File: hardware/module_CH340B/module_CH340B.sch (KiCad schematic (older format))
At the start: 5 parts, among them J1 USB-ID

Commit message: added usb input connections
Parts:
- J1: footprint (none) -> SquantorUsb:USB-muB-SMD_TH
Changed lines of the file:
@@
 F 0 "J1" H 1200 1250 50  0000 C CNN
 F 1 "USB-ID" H 1200 650 50  0000 C CNN
-F 2 "" H 1350 1000 60  0001 C CNN
+F 2 "SquantorUsb:USB-muB-SMD_TH" H 1350 1000 60  0001 C CNN
 F 3 "" H 1350 1000 60  0001 C CNN
 	1    1200 950

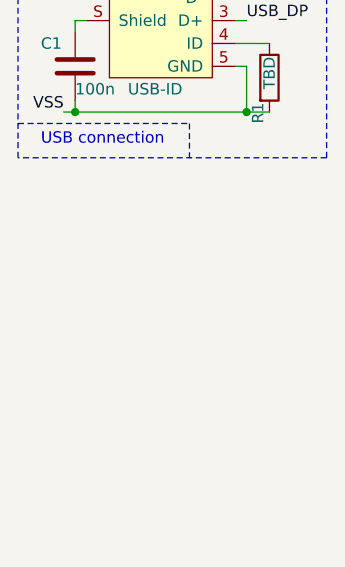
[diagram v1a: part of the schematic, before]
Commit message: added VBUS filtering
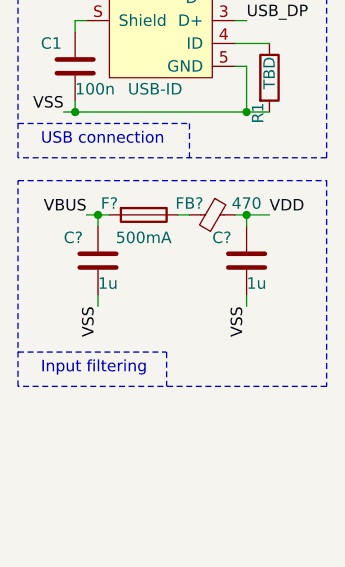
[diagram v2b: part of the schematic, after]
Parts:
- added C?: 1u, SquantorRcl:C_0603, symbol Device:C
- added C?: 1u, SquantorRcl:C_0805, symbol Device:C
- added F?: 500mA, SquantorRcl:R_0603_hand, symbol Device:Fuse
- added FB?: 470, SquantorRcl:L_0603, symbol Device:Ferrite_Bead_Small
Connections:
- net VBUS: now also C?.1, F?.2
- net VSS: now also C?.2, C?.2
- new net: F?.1, FB?.2
- new net VDD: C?.1, FB?.1
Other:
- note added: "Input filtering"
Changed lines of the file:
@@
 Wire Notes Line
 	1350 1400 1350 1550
+$Comp
+L Device:C C?
+U 1 1 5EE197E8
+P 950 2000
+F 0 "C?" H 800 2100 50  0000 L CNN
+F 1 "1u" H 950 1900 50  0000 L CNN
+F 2 "SquantorRcl:C_0603" H 988 1850 50  0001 C CNN
+F 3 "~" H 950 2000 50  0001 C CNN
+	1    950  2000
+	1    0    0    -1
+$EndComp
+$Comp
+L Device:Fuse F?
+U 1 1 5EE19F35
+P 1150 1800
+F 0 "F?" V 1100 1650 50  0000 C CNN
+F 1 "500mA" V 1250 1800 50  0000 C CNN
+F 2 "SquantorRcl:R_0603_hand" V 1080 1800 50  0001 C CNN
+F 3 "~" H 1150 1800 50  0001 C CNN
+	1    1150 1800
+	0    1    1    0
+$EndComp
+Text Label 950  2200 3    50   ~ 0
+VSS
+$Comp
+L Device:Ferrite_Bead_Small FB?
+U 1 1 5EE1ABAE
+P 1450 1800
+F 0 "FB?" V 1400 1700 50  0000 C CNN
+F 1 "470" V 1400 1950 50  0000 C CNN
+F 2 "SquantorRcl:L_0603" V 1380 1800 50  0001 C CNN
+F 3 "~" H 1450 1800 50  0001 C CNN
+	1    1450 1800
+	0    1    1    0
+$EndComp
+$Comp
+L Device:C C?
+U 1 1 5EE1B7FD
+P 1600 2000
+F 0 "C?" H 1450 2100 50  0000 L CNN
+F 1 "1u" H 1600 1900 50  0000 L CNN
+F 2 "SquantorRcl:C_0805" H 1638 1850 50  0001 C CNN
+F 3 "~" H 1600 2000 50  0001 C CNN
+	1    1600 2000
+	1    0    0    -1
+$EndComp
+Text Label 1600 2200 3    50   ~ 0
+VSS
+Text Label 900  1800 2    50   ~ 0
+VBUS
+Wire Wire Line
+	900  1800 950  1800
+Wire Wire Line
+	1300 1800 1350 1800
+Text Label 1700 1800 0    50   ~ 0
+VDD
+Wire Wire Line
+	1550 1800 1600 1800
+Wire Wire Line
+	1600 1850 1600 1800
+Connection ~ 1600 1800
+Wire Wire Line
+	1600 1800 1700 1800
+Wire Wire Line
+	950  2150 950  2200
+Wire Wire Line
+	1600 2200 1600 2150
+Wire Wire Line
+	950  1850 950  1800
+Connection ~ 950  1800
+Wire Wire Line
+	950  1800 1000 1800
+Text Notes 700  2500 0    50   ~ 0
+Input filtering
+Wire Notes Line
+	600  1650 1950 1650
+Wire Notes Line
+	1950 1650 1950 2550
+Wire Notes Line
+	1950 2550 600  2550
+Wire Notes Line
+	600  2550 600  1650
+Wire Notes Line
+	600  2400 1250 2400
+Wire Notes Line
+	1250 2400 1250 2550
 $EndSCHEMATC

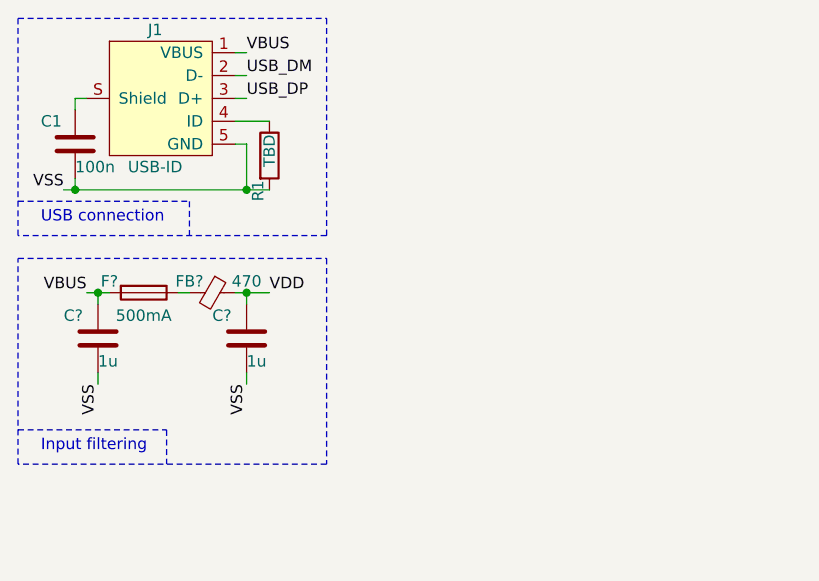
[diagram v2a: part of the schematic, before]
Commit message: added newer component library, minor schematic updates
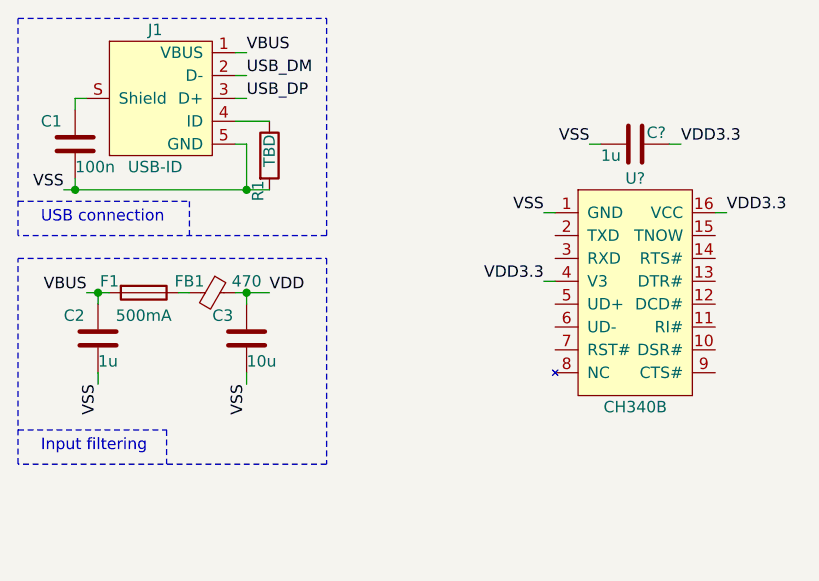
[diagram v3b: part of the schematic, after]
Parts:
- added C?: 1u, SquantorRcl:C_0603, symbol Device:C
- added U?: CH340B, symbol SquantorWCH:CH340B
- C3: renamed from C?; value 1u -> 10u
- gave numbers to parts that had none: 3
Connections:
- net VSS: now also C?.2, U?.1 (GND)
- new net VDD3.3: C?.1, U?.16 (VCC), U?.4 (V3)
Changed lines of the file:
@@
 	1350 1400 1350 1550
 $Comp
-L Device:C C?
+L Device:C C2
 U 1 1 5EE197E8
 P 950 2000
-F 0 "C?" H 800 2100 50  0000 L CNN
+F 0 "C2" H 800 2100 50  0000 L CNN
 F 1 "1u" H 950 1900 50  0000 L CNN
 F 2 "SquantorRcl:C_0603" H 988 1850 50  0001 C CNN
@@
 $EndComp
 $Comp
-L Device:Fuse F?
+L Device:Fuse F1
 U 1 1 5EE19F35
 P 1150 1800
-F 0 "F?" V 1100 1650 50  0000 C CNN
+F 0 "F1" V 1100 1650 50  0000 C CNN
 F 1 "500mA" V 1250 1800 50  0000 C CNN
 F 2 "SquantorRcl:R_0603_hand" V 1080 1800 50  0001 C CNN
@@
 VSS
 $Comp
-L Device:Ferrite_Bead_Small FB?
+L Device:Ferrite_Bead_Small FB1
 U 1 1 5EE1ABAE
 P 1450 1800
-F 0 "FB?" V 1400 1700 50  0000 C CNN
+F 0 "FB1" V 1400 1700 50  0000 C CNN
 F 1 "470" V 1400 1950 50  0000 C CNN
 F 2 "SquantorRcl:L_0603" V 1380 1800 50  0001 C CNN
@@
 $EndComp
 $Comp
-L Device:C C?
+L Device:C C3
 U 1 1 5EE1B7FD
 P 1600 2000
-F 0 "C?" H 1450 2100 50  0000 L CNN
-F 1 "1u" H 1600 1900 50  0000 L CNN
+F 0 "C3" H 1450 2100 50  0000 L CNN
+F 1 "10u" H 1600 1900 50  0000 L CNN
 F 2 "SquantorRcl:C_0805" H 1638 1850 50  0001 C CNN
 F 3 "~" H 1600 2000 50  0001 C CNN
@@
 Wire Notes Line
 	1250 2400 1250 2550
+$Comp
+L SquantorWCH:CH340B U?
+U 1 1 5EE21C28
+P 3300 1800
+F 0 "U?" H 3300 2300 50  0000 C CNN
+F 1 "CH340B" H 3300 1300 50  0000 C CNN
+F 2 "" H 3300 1800 50  0001 C CNN
+F 3 "" H 3300 1800 50  0001 C CNN
+	1    3300 1800
+	1    0    0    -1
+$EndComp
+Text Label 2900 1450 2    50   ~ 0
+VSS
+Text Label 3700 1450 0    50   ~ 0
+VDD3.3
+Text Label 2900 1750 2    50   ~ 0
+VDD3.3
+$Comp
+L Device:C C?
+U 1 1 5EE25876
+P 3300 1150
+F 0 "C?" V 3250 1200 50  0000 L CNN
+F 1 "1u" V 3350 1000 50  0000 L CNN
+F 2 "SquantorRcl:C_0603" H 3338 1000 50  0001 C CNN
+F 3 "~" H 3300 1150 50  0001 C CNN
+	1    3300 1150
+	0    1    1    0
+$EndComp
+Text Label 3100 1150 2    50   ~ 0
+VSS
+Text Label 3500 1150 0    50   ~ 0
+VDD3.3
+Wire Wire Line
+	2900 1450 2950 1450
+Wire Wire Line
+	2900 1750 2950 1750
+Wire Wire Line
+	3100 1150 3150 1150
+Wire Wire Line
+	3450 1150 3500 1150
+Wire Wire Line
+	3650 1450 3700 1450
 $EndSCHEMATC

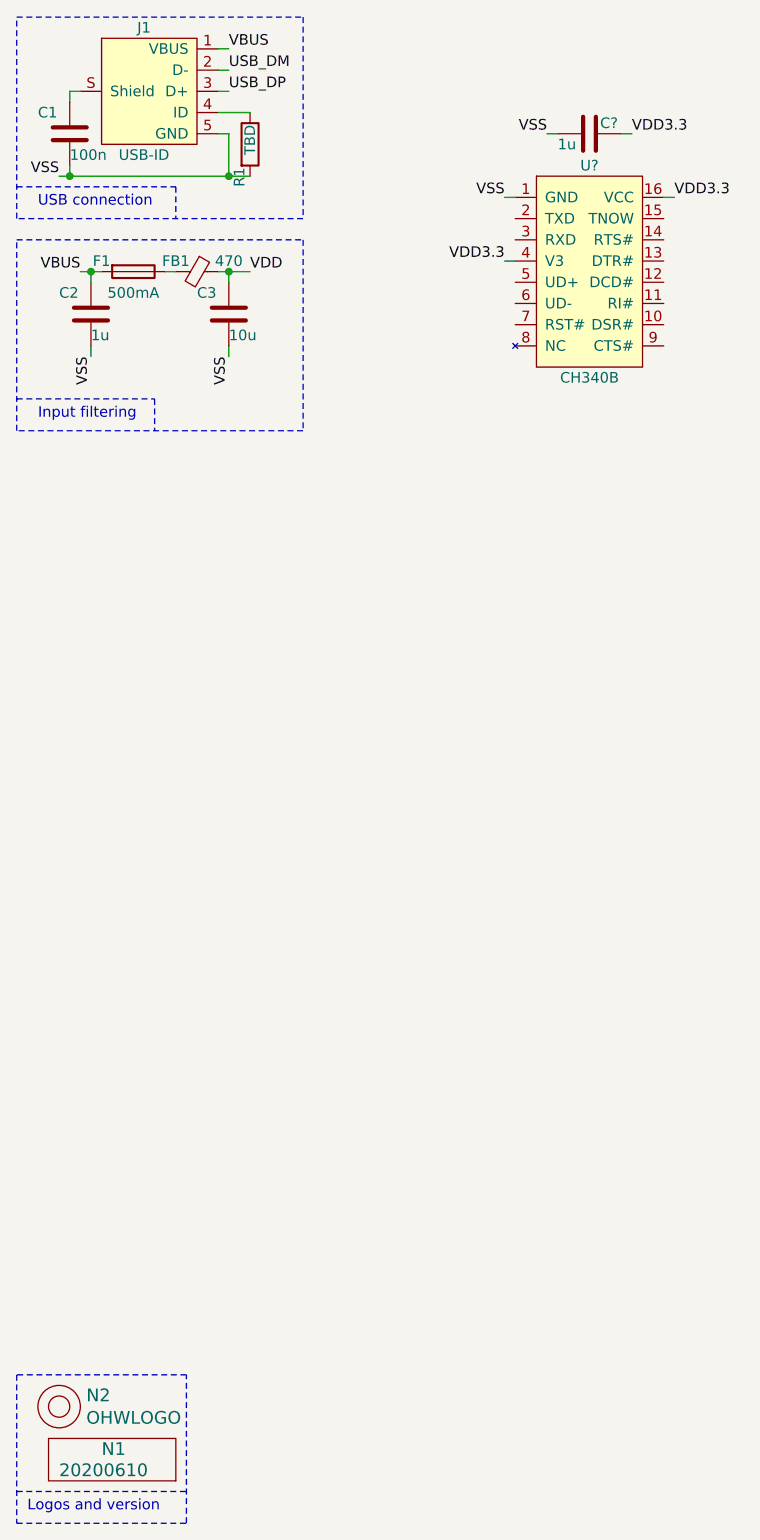
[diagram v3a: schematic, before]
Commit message: added regulator and USB to serial converter
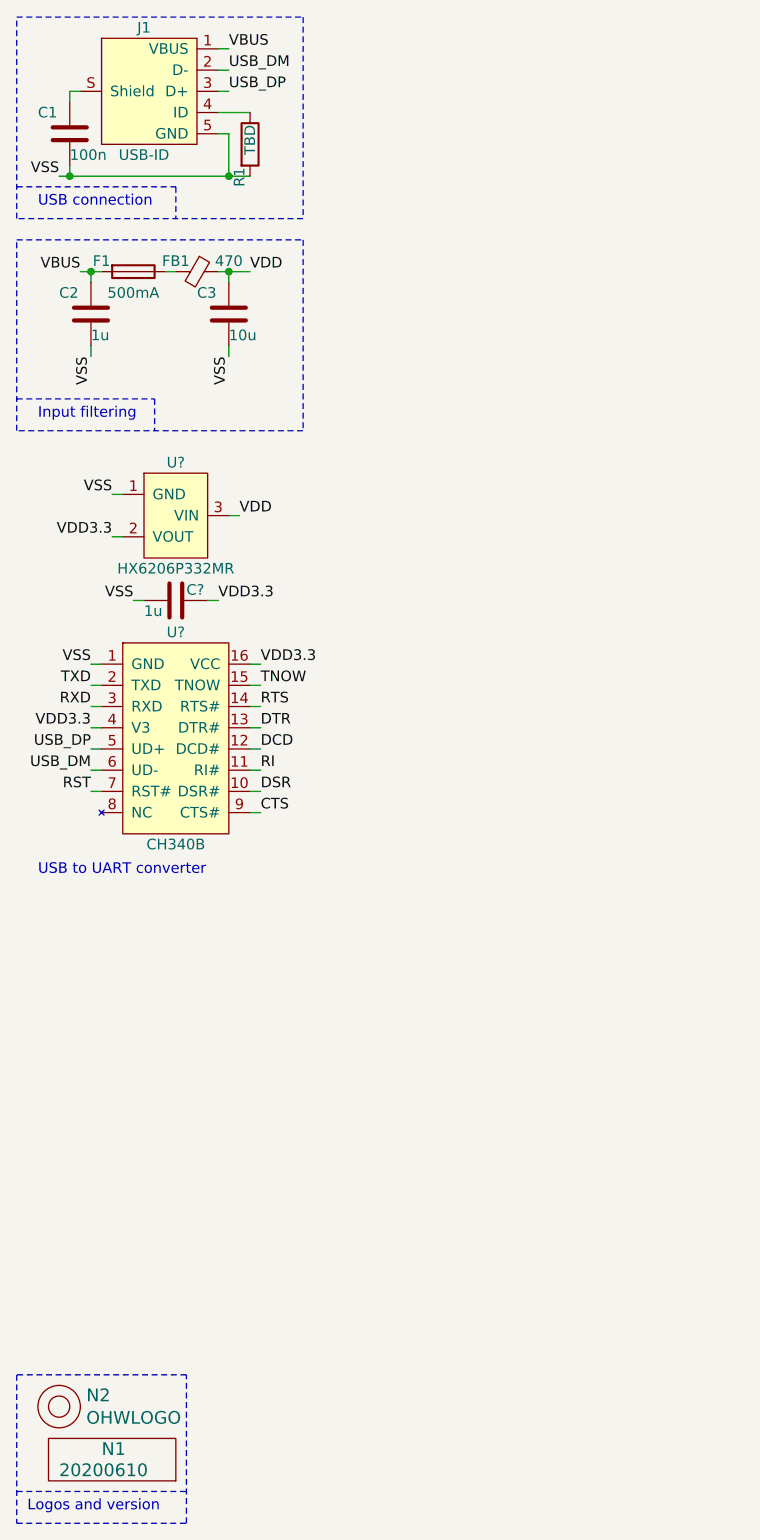
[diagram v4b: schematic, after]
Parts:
- added U?: HX6206P332MR, SquantorIC:SOT23-3, symbol SquantorGenericAnalog:regulator_sot23
- U?: footprint (none) -> Package_SO:SO-16_5.3x10.2mm_P1.27mm
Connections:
- net USB_DM: now also U?.6 (UD-)
- net USB_DP: now also U?.5 (UD+)
- net VDD: now also U?.3 (VIN)
- net VDD3.3: now also U?.2 (VOUT)
- net VSS: now also U?.1 (GND)
- net DSR: now reaches U?.10 (DSR#)
- net RI: now reaches U?.11 (RI#)
- net DCD: now reaches U?.12 (DCD#)
- net DTR: now reaches U?.13 (DTR#)
- net RTS: now reaches U?.14 (RTS#)
- net TNOW: now reaches U?.15 (TNOW)
- net TXD: now reaches U?.2 (TXD)
- net RXD: now reaches U?.3 (RXD)
- net RST: now reaches U?.7 (RST#)
- net CTS: now reaches U?.9 (CTS#)
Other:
- note added: "USB to UART converter"
- moved on the sheet: C?, U?
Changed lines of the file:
@@
 L SquantorWCH:CH340B U?
 U 1 1 5EE21C28
-P 3300 1800
-F 0 "U?" H 3300 2300 50  0000 C CNN
-F 1 "CH340B" H 3300 1300 50  0000 C CNN
-F 2 "" H 3300 1800 50  0001 C CNN
-F 3 "" H 3300 1800 50  0001 C CNN
-	1    3300 1800
+P 1350 4000
+F 0 "U?" H 1350 4500 50  0000 C CNN
+F 1 "CH340B" H 1350 3500 50  0000 C CNN
+F 2 "Package_SO:SO-16_5.3x10.2mm_P1.27mm" H 1350 4000 50  0001 C CNN
+F 3 "" H 1350 4000 50  0001 C CNN
+	1    1350 4000
 	1    0    0    -1
 $EndComp
-Text Label 2900 1450 2    50   ~ 0
+Text Label 950  3650 2    50   ~ 0
 VSS
-Text Label 3700 1450 0    50   ~ 0
+Text Label 1750 3650 0    50   ~ 0
 VDD3.3
-Text Label 2900 1750 2    50   ~ 0
+Text Label 950  3950 2    50   ~ 0
 VDD3.3
 $Comp
 L Device:C C?
 U 1 1 5EE25876
-P 3300 1150
-F 0 "C?" V 3250 1200 50  0000 L CNN
-F 1 "1u" V 3350 1000 50  0000 L CNN
-F 2 "SquantorRcl:C_0603" H 3338 1000 50  0001 C CNN
-F 3 "~" H 3300 1150 50  0001 C CNN
-	1    3300 1150
+P 1350 3350
+F 0 "C?" V 1300 3400 50  0000 L CNN
+F 1 "1u" V 1400 3200 50  0000 L CNN
+F 2 "SquantorRcl:C_0603" H 1388 3200 50  0001 C CNN
+F 3 "~" H 1350 3350 50  0001 C CNN
+	1    1350 3350
 	0    1    1    0
 $EndComp
-Text Label 3100 1150 2    50   ~ 0
+Text Label 1150 3350 2    50   ~ 0
 VSS
-Text Label 3500 1150 0    50   ~ 0
+Text Label 1550 3350 0    50   ~ 0
 VDD3.3
 Wire Wire Line
-	2900 1450 2950 1450
+	950  3650 1000 3650
 Wire Wire Line
-	2900 1750 2950 1750
+	950  3950 1000 3950
 Wire Wire Line
-	3100 1150 3150 1150
+	1150 3350 1200 3350
 Wire Wire Line
-	3450 1150 3500 1150
+	1500 3350 1550 3350
 Wire Wire Line
-	3650 1450 3700 1450
+	1700 3650 1750 3650
+$Comp
+L SquantorGenericAnalog:regulator_sot23 U?
+U 1 1 5EE2E2C4
+P 1350 2950
+F 0 "U?" H 1350 3200 50  0000 C CNN
+F 1 "HX6206P332MR" H 1350 2700 50  0000 C CNN
+F 2 "SquantorIC:SOT23-3" H 1350 2950 50  0001 C CNN
+F 3 "" H 1350 2950 50  0001 C CNN
+	1    1350 2950
+	1    0    0    -1
+$EndComp
+Text Label 1050 2850 2    50   ~ 0
+VSS
+Text Label 1050 3050 2    50   ~ 0
+VDD3.3
+Text Label 1650 2950 0    50   ~ 0
+VDD
+Text Notes 700  4650 0    50   ~ 0
+USB to UART converter
+Wire Wire Line
+	1050 2850 1100 2850
+Wire Wire Line
+	1100 3050 1050 3050
+Wire Wire Line
+	1650 2950 1600 2950
+Text Label 950  3750 2    50   ~ 0
+TXD
+Text Label 950  3850 2    50   ~ 0
+RXD
+Text Label 950  4150 2    50   ~ 0
+USB_DM
+Text Label 950  4050 2    50   ~ 0
+USB_DP
+Text Label 950  4250 2    50   ~ 0
+RST
+Text Label 1750 4350 0    50   ~ 0
+CTS
+Text Label 1750 4250 0    50   ~ 0
+DSR
+Text Label 1750 4150 0    50   ~ 0
+RI
+Text Label 1750 4050 0    50   ~ 0
+DCD
+Text Label 1750 3950 0    50   ~ 0
+DTR
+Text Label 1750 3850 0    50   ~ 0
+RTS
+Text Label 1750 3750 0    50   ~ 0
+TNOW
+Wire Wire Line
+	950  3750 1000 3750
+Wire Wire Line
+	1000 3850 950  3850
+Wire Wire Line
+	950  4050 1000 4050
+Wire Wire Line
+	1000 4150 950  4150
+Wire Wire Line
+	950  4250 1000 4250
+Wire Wire Line
+	1700 4350 1750 4350
+Wire Wire Line
+	1750 4250 1700 4250
+Wire Wire Line
+	1700 4150 1750 4150
+Wire Wire Line
+	1750 4050 1700 4050
+Wire Wire Line
+	1700 3950 1750 3950
+Wire Wire Line
+	1750 3850 1700 3850
+Wire Wire Line
+	1700 3750 1750 3750
 $EndSCHEMATC

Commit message: annotation completed
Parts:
- gave numbers to parts that had none: 3
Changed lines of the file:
@@
 	1250 2400 1250 2550
 $Comp
-L SquantorWCH:CH340B U?
+L SquantorWCH:CH340B U2
 U 1 1 5EE21C28
 P 1350 4000
-F 0 "U?" H 1350 4500 50  0000 C CNN
+F 0 "U2" H 1350 4500 50  0000 C CNN
 F 1 "CH340B" H 1350 3500 50  0000 C CNN
 F 2 "Package_SO:SO-16_5.3x10.2mm_P1.27mm" H 1350 4000 50  0001 C CNN
@@
 VDD3.3
 $Comp
-L Device:C C?
+L Device:C C4
 U 1 1 5EE25876
 P 1350 3350
-F 0 "C?" V 1300 3400 50  0000 L CNN
+F 0 "C4" V 1300 3400 50  0000 L CNN
 F 1 "1u" V 1400 3200 50  0000 L CNN
 F 2 "SquantorRcl:C_0603" H 1388 3200 50  0001 C CNN
@@
 	1700 3650 1750 3650
 $Comp
-L SquantorGenericAnalog:regulator_sot23 U?
+L SquantorGenericAnalog:regulator_sot23 U1
 U 1 1 5EE2E2C4
 P 1350 2950
-F 0 "U?" H 1350 3200 50  0000 C CNN
+F 0 "U1" H 1350 3200 50  0000 C CNN
 F 1 "HX6206P332MR" H 1350 2700 50  0000 C CNN
 F 2 "SquantorIC:SOT23-3" H 1350 2950 50  0001 C CNN
@@
 Text Label 1650 2950 0    50   ~ 0
 VDD
-Text Notes 700  4650 0    50   ~ 0
+Text Notes 650  4900 0    50   ~ 0
 USB to UART converter
 Wire Wire Line
